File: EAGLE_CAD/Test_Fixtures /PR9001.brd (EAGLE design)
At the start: 62.5 x 42.5 mm, 9 parts, among them T10 PR9001_TESTPOINT, T11 PR9001_TESTPOINT, T12 PR9001_TESTPOINT, T13 PR9001_TESTPOINT, T2 PR9001_TESTPOINT, T3 PR9001_TESTPOINT, T4 PR9001_TESTPOINT, T5 PR9001_TESTPOINT

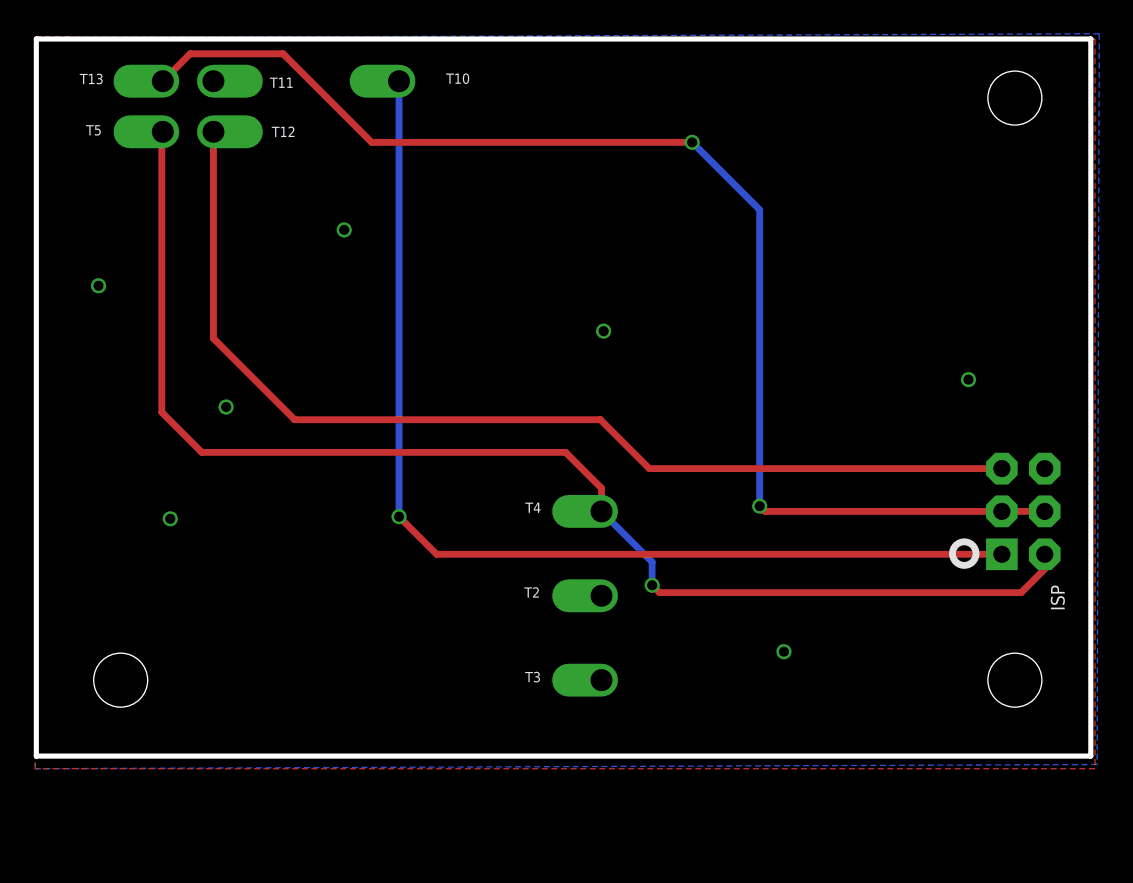
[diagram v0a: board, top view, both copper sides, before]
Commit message: PR9001
added pass / fail LEDs
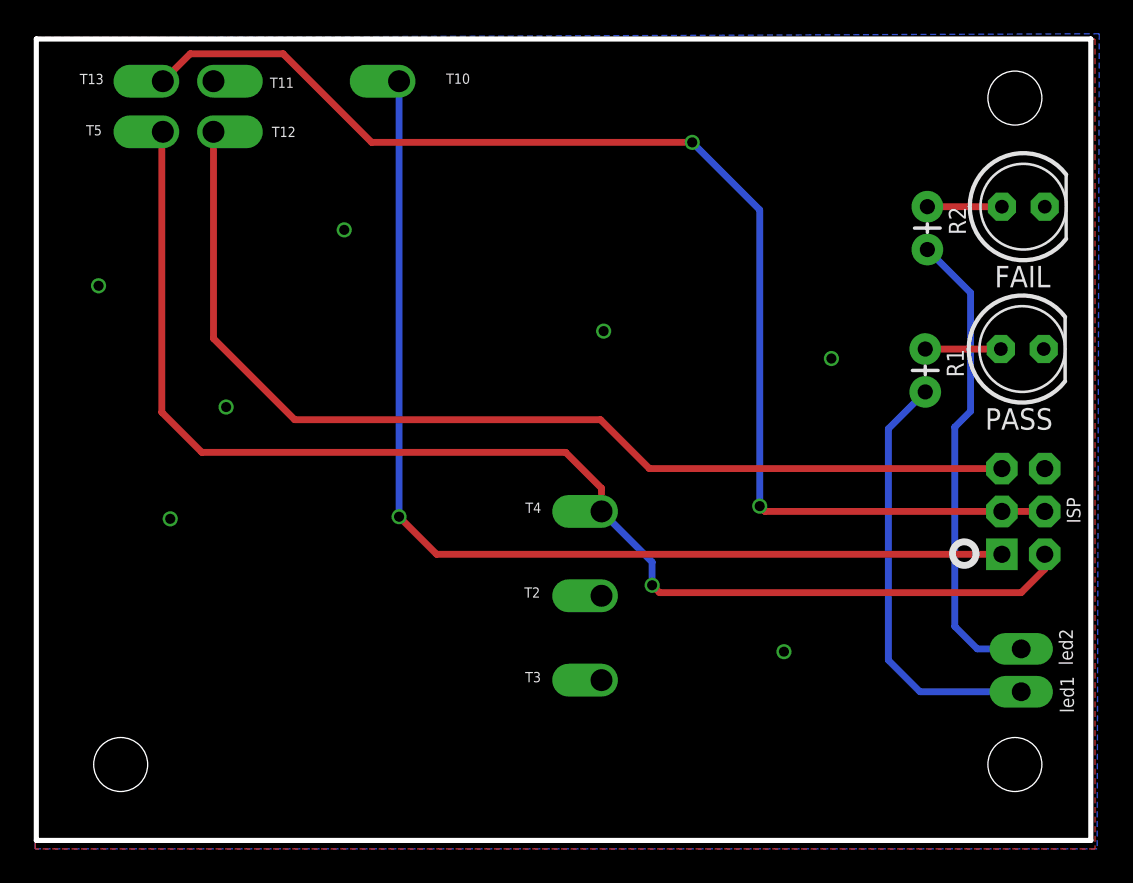
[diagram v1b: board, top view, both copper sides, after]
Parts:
- added FAIL, PASS: (no value), adafruit:LED5MM
- added JP1: M02PTH3, SparkFun-Connectors:1X02_LONGPADS
- added R1, R2: (no value), SparkFun-Resistors:AXIAL-0.1
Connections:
- new net N$1: JP1.2, R2.P$2
- new net N$2: PASS.A, R1.P$1
- new net N$3: JP1.1, R1.P$2
- new net N$4: FAIL.A, R2.P$1
- net GND: now also FAIL.K, PASS.K
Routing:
- net N$1: track 0.00 -> 28.3 mm
- net N$3: track 0.00 -> 25.5 mm
- net N$2: track 0.00 -> 4.48 mm
- net N$4: track 0.00 -> 4.42 mm
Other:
- board size 62.5 x 42.5 mm -> 62.5 x 47.5 mm
- board text added: "led1"
- board text added: "led2"
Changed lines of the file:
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@@
 <plain>
 <wire x1="25.5" y1="68" x2="88" y2="68" width="0.3048" layer="20"/>
-<wire x1="88" y1="68" x2="88" y2="25.5" width="0.3048" layer="20"/>
-<wire x1="88" y1="25.5" x2="25.5" y2="25.5" width="0.3048" layer="20"/>
-<wire x1="25.5" y1="25.5" x2="25.5" y2="68" width="0.3048" layer="20"/>
-<hole x="30.5" y="30" drill="3.2"/>
-<hole x="83.5" y="30" drill="3.2"/>
+<wire x1="88" y1="68" x2="88" y2="20.5" width="0.3048" layer="20"/>
+<wire x1="88" y1="20.5" x2="25.5" y2="20.5" width="0.3048" layer="20"/>
+<wire x1="25.5" y1="20.5" x2="25.5" y2="68" width="0.3048" layer="20"/>
+<hole x="30.5" y="25" drill="3.2"/>
+<hole x="83.5" y="25" drill="3.2"/>
 <hole x="83.5" y="64.5" drill="3.2"/>
 <circle x="80.5" y="37.5" radius="0.69876875" width="0.4064" layer="25"/>
+<text x="87" y="28.0625" size="0.8128" layer="25" rot="R90">led1</text>
+<text x="86.9375" y="30.875" size="0.8128" layer="25" rot="R90">led2</text>
 </plain>
 <attributes>
@@
 <elements>
 <element name="ISP" library="PR_Parts_Library" package="2X3-NS" value="" x="84" y="40" smashed="yes" rot="MR90">
-<attribute name="NAME" x="86.45" y="34.1025" size="0.8128" layer="25" font="vector" ratio="16" rot="R90"/>
+<attribute name="NAME" x="87.3875" y="39.29" size="0.8128" layer="25" font="vector" ratio="16" rot="R90"/>
 <attribute name="VALUE" x="85.255" y="34.94" size="1.27" layer="28" rot="MR0"/>
 <attribute name="MFG_PN" value="M20-9980346" x="84" y="40" size="1.778" layer="28" rot="MR90" display="off"/>
@@
 <attribute name="VALUE" x="33.508" y="64.738" size="0.254" layer="28" rot="MR0"/>
 </element>
+<element name="PASS" library="adafruit" package="LED5MM" value="" x="83.9375" y="49.625" smashed="yes">
+<attribute name="NAME" x="81.7375" y="44.8459" size="1.27" layer="25" ratio="10"/>
+<attribute name="VALUE" x="87.1379" y="47.8216" size="1.27" layer="27" ratio="10"/>
+</element>
+<element name="FAIL" library="adafruit" package="LED5MM" value="" x="84" y="58.0625" smashed="yes">
+<attribute name="NAME" x="82.3" y="53.2834" size="1.27" layer="25" ratio="10"/>
+<attribute name="VALUE" x="87.2004" y="56.2591" size="1.27" layer="27" ratio="10"/>
+</element>
+<element name="JP1" library="SparkFun-Connectors" package="1X02_LONGPADS" value="M02PTH3" x="83.875" y="29.3125" rot="R90"/>
+<element name="R1" library="SparkFun-Resistors" package="AXIAL-0.1" value="" x="78.1875" y="49.625" rot="R270"/>
+<element name="R2" library="SparkFun-Resistors" package="AXIAL-0.1" value="" x="78.3125" y="58.0625" rot="R270"/>
 </elements>
 <signals>
@@
 <vertex x="25.5625" y="68.0625"/>
 <vertex x="88.5" y="68.3125"/>
-<vertex x="88.375" y="25"/>
-<vertex x="25.4375" y="24.75"/>
+<vertex x="88.375" y="20"/>
+<vertex x="25.4375" y="20"/>
 </polygon>
 <polygon width="0.3048" layer="1">
 <vertex x="25.4375" y="68.125"/>
 <vertex x="88.25" y="68"/>
-<vertex x="88.25" y="24.75"/>
-<vertex x="25.4375" y="24.75"/>
+<vertex x="88.25" y="20"/>
+<vertex x="25.4375" y="20"/>
 </polygon>
 <via x="29.1875" y="53.375" extent="1-16" drill="0.6"/>
@@
 <via x="36.75" y="46.1875" extent="1-16" drill="0.6"/>
 <via x="33.4375" y="39.5625" extent="1-16" drill="0.6"/>
-<via x="80.75" y="47.8125" extent="1-16" drill="0.6"/>
+<via x="72.625" y="49.0625" extent="1-16" drill="0.6"/>
 <via x="59.125" y="50.6875" extent="1-16" drill="0.6"/>
 <via x="69.8125" y="31.6875" extent="1-16" drill="0.6"/>
+<contactref element="FAIL" pad="K"/>
+<contactref element="PASS" pad="K"/>
 </signal>
 <signal name="!RST">
@@
 </polygon>
 </signal>
+<signal name="N$2">
+<contactref element="R1" pad="P$1"/>
+<contactref element="PASS" pad="A"/>
+<wire x1="78.1875" y1="49.625" x2="82.6675" y2="49.625" width="0.4064" layer="1"/>
+</signal>
+<signal name="N$4">
+<contactref element="R2" pad="P$1"/>
+<contactref element="FAIL" pad="A"/>
+<wire x1="78.3125" y1="58.0625" x2="82.73" y2="58.0625" width="0.4064" layer="1"/>
+</signal>
+<signal name="N$1">
+<contactref element="JP1" pad="2"/>
+<contactref element="R2" pad="P$2"/>
+<wire x1="83.875" y1="31.8525" x2="81.2725" y2="31.8525" width="0.4064" layer="16"/>
+<wire x1="81.2725" y1="31.8525" x2="79.9375" y2="33.1875" width="0.4064" layer="16"/>
+<wire x1="79.9375" y1="33.1875" x2="79.9375" y2="45" width="0.4064" layer="16"/>
+<wire x1="79.9375" y1="45" x2="80.875" y2="45.9375" width="0.4064" layer="16"/>
+<wire x1="80.875" y1="45.9375" x2="80.875" y2="52.96" width="0.4064" layer="16"/>
+<wire x1="80.875" y1="52.96" x2="78.3125" y2="55.5225" width="0.4064" layer="16"/>
+</signal>
+<signal name="N$3">
+<contactref element="JP1" pad="1"/>
+<contactref element="R1" pad="P$2"/>
+<wire x1="83.875" y1="29.3125" x2="77.875" y2="29.3125" width="0.4064" layer="16"/>
+<wire x1="77.875" y1="29.3125" x2="76" y2="31.1875" width="0.4064" layer="16"/>
+<wire x1="76" y1="31.1875" x2="76" y2="44.8975" width="0.4064" layer="16"/>
+<wire x1="76" y1="44.8975" x2="78.1875" y2="47.085" width="0.4064" layer="16"/>
+</signal>
 </signals>
